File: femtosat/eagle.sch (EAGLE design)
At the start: 21 parts, among them U1 ATMEGA328P_TQFP, U2 915MHz, U3 3.3V/150mA, U4 9DoF IMU, U5 BME280, Y1 16MHz

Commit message: Finished Connecting Sensors
Very unsure if this will work, need to ask lots of questions
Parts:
- added C4, C5: 0.1uF, femtosat:CAPACITOR_0.1UF
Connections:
- removed net N$22: R3.1, TP2.1, U1.PC4(ADC4/SDA)
- removed net N$23: R4.1, TP1.1, U1.PC5(ADC5/SCL)
- removed net N$8: U1.PD2(INT0), U2.DIO0
- new net INT: U1.PD2(INT0), U2.DIO0, U4.INT
- new net N$18: C5.2, U4.REGOUT
- new net SCL: R4.1, TP1.1, U1.PC5(ADC5/SCL), U4.SCL/SCLK, U5.SCK/SCL
- new net SDA: R3.1, TP2.1, U1.PC4(ADC4/SDA), U4.SDA/SDI, U5.SDI/SDA
- net 3.3V: now also C4.2, U4.!CS, U4.VDDIO, U5.!CS, U5.VDDIO
- net GND: now also C4.1, C5.1, U4.AD0/SDO, U4.FSYNC, U5.SDO/ADR
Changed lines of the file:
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@@
 <part name="TP1" library="femtosat" deviceset="TEST-POINT" device="3"/>
 <part name="TP2" library="femtosat" deviceset="TEST-POINT" device="3"/>
+<part name="C4" library="femtosat" deviceset="CAPACITOR_0.1UF" device="" value="0.1uF"/>
+<part name="C5" library="femtosat" deviceset="CAPACITOR_0.1UF" device="" value="0.1uF"/>
 </parts>
 <sheets>
@@
 <attribute name="NAME" x="162.56" y="137.16" size="1.778" layer="95" font="vector" rot="R90"/>
 <attribute name="VALUE" x="167.64" y="137.16" size="1.778" layer="96" font="vector" rot="R90"/>
+</instance>
+<instance part="C4" gate="G$1" x="20.32" y="43.18" smashed="yes" rot="R180">
+<attribute name="NAME" x="18.796" y="40.259" size="1.778" layer="95" font="vector" rot="R180"/>
+<attribute name="VALUE" x="18.796" y="45.339" size="1.778" layer="96" font="vector" rot="R180"/>
+</instance>
+<instance part="C5" gate="G$1" x="25.4" y="30.48" smashed="yes" rot="R180">
+<attribute name="NAME" x="23.876" y="27.559" size="1.778" layer="95" font="vector" rot="R180"/>
+<attribute name="VALUE" x="23.876" y="32.639" size="1.778" layer="96" font="vector" rot="R180"/>
 </instance>
 </instances>
@@
 <pinref part="U4" gate="G$1" pin="GND"/>
 <wire x1="40.64" y1="35.56" x2="30.48" y2="35.56" width="0.1524" layer="91"/>
-<wire x1="30.48" y1="35.56" x2="30.48" y2="20.32" width="0.1524" layer="91"/>
+<wire x1="30.48" y1="35.56" x2="30.48" y2="25.4" width="0.1524" layer="91"/>
 <pinref part="GND9" gate="1" pin="GND"/>
+<pinref part="C4" gate="G$1" pin="1"/>
+<wire x1="30.48" y1="25.4" x2="30.48" y2="20.32" width="0.1524" layer="91"/>
+<wire x1="20.32" y1="38.1" x2="20.32" y2="35.56" width="0.1524" layer="91"/>
+<wire x1="20.32" y1="35.56" x2="30.48" y2="35.56" width="0.1524" layer="91"/>
+<junction x="30.48" y="35.56"/>
+<pinref part="U4" gate="G$1" pin="AD0/SDO"/>
+<wire x1="76.2" y1="35.56" x2="81.28" y2="35.56" width="0.1524" layer="91"/>
+<wire x1="81.28" y1="35.56" x2="81.28" y2="25.4" width="0.1524" layer="91"/>
+<wire x1="81.28" y1="25.4" x2="30.48" y2="25.4" width="0.1524" layer="91"/>
+<junction x="30.48" y="25.4"/>
+<pinref part="C5" gate="G$1" pin="1"/>
+<wire x1="25.4" y1="25.4" x2="30.48" y2="25.4" width="0.1524" layer="91"/>
+<pinref part="U4" gate="G$1" pin="FSYNC"/>
+<wire x1="40.64" y1="40.64" x2="30.48" y2="40.64" width="0.1524" layer="91"/>
+<wire x1="30.48" y1="40.64" x2="30.48" y2="35.56" width="0.1524" layer="91"/>
 </segment>
 <segment>
 <pinref part="U5" gate="U1" pin="GND"/>
 <wire x1="25.4" y1="91.44" x2="20.32" y2="91.44" width="0.1524" layer="91"/>
-<wire x1="20.32" y1="91.44" x2="20.32" y2="81.28" width="0.1524" layer="91"/>
+<wire x1="20.32" y1="91.44" x2="20.32" y2="83.82" width="0.1524" layer="91"/>
 <pinref part="GND10" gate="1" pin="GND"/>
+<pinref part="U5" gate="U1" pin="SDO/ADR"/>
+<wire x1="20.32" y1="83.82" x2="20.32" y2="81.28" width="0.1524" layer="91"/>
+<wire x1="53.34" y1="91.44" x2="58.42" y2="91.44" width="0.1524" layer="91"/>
+<wire x1="58.42" y1="91.44" x2="58.42" y2="83.82" width="0.1524" layer="91"/>
+<wire x1="58.42" y1="83.82" x2="20.32" y2="83.82" width="0.1524" layer="91"/>
+<junction x="20.32" y="83.82"/>
 </segment>
 </net>
@@
 <pinref part="U4" gate="G$1" pin="VDD"/>
 <wire x1="40.64" y1="48.26" x2="30.48" y2="48.26" width="0.1524" layer="91"/>
-<wire x1="30.48" y1="48.26" x2="30.48" y2="58.42" width="0.1524" layer="91"/>
+<wire x1="30.48" y1="48.26" x2="30.48" y2="55.88" width="0.1524" layer="91"/>
 <pinref part="P+4" gate="G$1" pin="3.3V"/>
+<pinref part="U4" gate="G$1" pin="VDDIO"/>
+<wire x1="30.48" y1="55.88" x2="30.48" y2="58.42" width="0.1524" layer="91"/>
+<wire x1="40.64" y1="45.72" x2="30.48" y2="45.72" width="0.1524" layer="91"/>
+<wire x1="30.48" y1="45.72" x2="30.48" y2="48.26" width="0.1524" layer="91"/>
+<junction x="30.48" y="48.26"/>
+<pinref part="C4" gate="G$1" pin="2"/>
+<wire x1="30.48" y1="48.26" x2="20.32" y2="48.26" width="0.1524" layer="91"/>
+<wire x1="20.32" y1="48.26" x2="20.32" y2="45.72" width="0.1524" layer="91"/>
+<pinref part="U4" gate="G$1" pin="!CS"/>
+<wire x1="76.2" y1="43.18" x2="81.28" y2="43.18" width="0.1524" layer="91"/>
+<wire x1="81.28" y1="43.18" x2="81.28" y2="55.88" width="0.1524" layer="91"/>
+<wire x1="81.28" y1="55.88" x2="30.48" y2="55.88" width="0.1524" layer="91"/>
+<junction x="30.48" y="55.88"/>
 </segment>
 <segment>
 <pinref part="U5" gate="U1" pin="VDD"/>
 <wire x1="25.4" y1="104.14" x2="20.32" y2="104.14" width="0.1524" layer="91"/>
-<wire x1="20.32" y1="104.14" x2="20.32" y2="114.3" width="0.1524" layer="91"/>
+<wire x1="20.32" y1="104.14" x2="20.32" y2="109.22" width="0.1524" layer="91"/>
 <pinref part="P+5" gate="G$1" pin="3.3V"/>
+<pinref part="U5" gate="U1" pin="VDDIO"/>
+<wire x1="20.32" y1="109.22" x2="20.32" y2="114.3" width="0.1524" layer="91"/>
+<wire x1="25.4" y1="99.06" x2="20.32" y2="99.06" width="0.1524" layer="91"/>
+<wire x1="20.32" y1="99.06" x2="20.32" y2="104.14" width="0.1524" layer="91"/>
+<junction x="20.32" y="104.14"/>
+<pinref part="U5" gate="U1" pin="!CS"/>
+<wire x1="53.34" y1="104.14" x2="55.88" y2="104.14" width="0.1524" layer="91"/>
+<wire x1="55.88" y1="104.14" x2="55.88" y2="109.22" width="0.1524" layer="91"/>
+<wire x1="55.88" y1="109.22" x2="20.32" y2="109.22" width="0.1524" layer="91"/>
+<junction x="20.32" y="109.22"/>
 </segment>
 <segment>
@@
 </segment>
 </net>
-<net name="N$8" class="0">
+<net name="INT" class="0">
 <segment>
 <pinref part="U1" gate="U$1" pin="PD2(INT0)"/>
@@
 <pinref part="U2" gate="G$1" pin="DIO0"/>
 <wire x1="213.36" y1="96.52" x2="208.28" y2="96.52" width="0.1524" layer="91"/>
+<wire x1="213.36" y1="101.6" x2="220.98" y2="101.6" width="0.1524" layer="91"/>
+<junction x="213.36" y="101.6"/>
+<label x="220.98" y="101.6" size="1.778" layer="95"/>
+</segment>
+<segment>
+<pinref part="U4" gate="G$1" pin="INT"/>
+<wire x1="40.64" y1="43.18" x2="33.02" y2="43.18" width="0.1524" layer="91"/>
+<label x="30.48" y="43.18" size="1.778" layer="95"/>
 </segment>
 </net>
@@
 </segment>
 </net>
-<net name="N$22" class="0">
+<net name="SDA" class="0">
 <segment>
 <pinref part="U1" gate="U$1" pin="PC4(ADC4/SDA)"/>
 <wire x1="154.94" y1="129.54" x2="165.1" y2="129.54" width="0.1524" layer="91"/>
-<wire x1="165.1" y1="129.54" x2="177.8" y2="129.54" width="0.1524" layer="91"/>
+<wire x1="165.1" y1="129.54" x2="172.72" y2="129.54" width="0.1524" layer="91"/>
+<wire x1="172.72" y1="129.54" x2="177.8" y2="129.54" width="0.1524" layer="91"/>
 <wire x1="177.8" y1="129.54" x2="177.8" y2="139.7" width="0.1524" layer="91"/>
 <pinref part="R3" gate="G$1" pin="1"/>
@@
 <wire x1="165.1" y1="139.7" x2="165.1" y2="129.54" width="0.1524" layer="91"/>
 <junction x="165.1" y="129.54"/>
-</segment>
-</net>
-<net name="N$23" class="0">
+<wire x1="172.72" y1="129.54" x2="172.72" y2="134.62" width="0.1524" layer="91"/>
+<junction x="172.72" y="129.54"/>
+<label x="172.72" y="134.62" size="1.778" layer="95" rot="R90"/>
+</segment>
+<segment>
+<pinref part="U4" gate="G$1" pin="SDA/SDI"/>
+<wire x1="76.2" y1="38.1" x2="86.36" y2="38.1" width="0.1524" layer="91"/>
+<label x="86.36" y="38.1" size="1.778" layer="95"/>
+</segment>
+<segment>
+<pinref part="U5" gate="U1" pin="SDI/SDA"/>
+<wire x1="53.34" y1="99.06" x2="58.42" y2="99.06" width="0.1524" layer="91"/>
+<label x="58.42" y="99.06" size="1.778" layer="95"/>
+</segment>
+</net>
+<net name="SCL" class="0">
 <segment>
 <pinref part="U1" gate="U$1" pin="PC5(ADC5/SCL)"/>
@@
 <wire x1="187.96" y1="134.62" x2="187.96" y2="127" width="0.1524" layer="91"/>
 <junction x="187.96" y="127"/>
-</segment>
-</net>
+<wire x1="195.58" y1="127" x2="203.2" y2="127" width="0.1524" layer="91"/>
+<junction x="195.58" y="127"/>
+<label x="203.2" y="127" size="1.778" layer="95"/>
+</segment>
+<segment>
+<pinref part="U4" gate="G$1" pin="SCL/SCLK"/>
+<wire x1="76.2" y1="40.64" x2="86.36" y2="40.64" width="0.1524" layer="91"/>
+<label x="86.36" y="40.64" size="1.778" layer="95"/>
+</segment>
+<segment>
+<pinref part="U5" gate="U1" pin="SCK/SCL"/>
+<wire x1="53.34" y1="96.52" x2="58.42" y2="96.52" width="0.1524" layer="91"/>
+<label x="58.42" y="96.52" size="1.778" layer="95"/>
+</segment>
+</net>
+<net name="N$18" class="0">
+<segment>
+<pinref part="U4" gate="G$1" pin="REGOUT"/>
+<wire x1="40.64" y1="38.1" x2="25.4" y2="38.1" width="0.1524" layer="91"/>
+<pinref part="C5" gate="G$1" pin="2"/>
+<wire x1="25.4" y1="38.1" x2="25.4" y2="33.02" width="0.1524" layer="91"/>
+</segment>
+</net>

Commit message: Corrected Capacitors and Resistors
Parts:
- added C6, C7: 0.1uF, femtosat:CAPACITOR_0.1UF
- added R10, R8, R9: 10K, femtosat:RESISTOR_10KOHM0603
- added R11, R6, R7: 4.7k, femtosat:RESISTOR_4.7KOHM-0603-1/10W-1%
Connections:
- new net N$16: R11.2, U5.!CS
- new net N$8: R8.1, U4.!CS
- net 3.3V: now also C6.1, C7.1, R10.2, R11.1, R6.2, R7.2, R8.2, R9.2; no longer U4.!CS, U5.!CS
- net GND: now also C6.2, C7.2, U4.INT
- net INT: no longer U4.INT
- net SCL: now also R6.1, R9.1
- net SDA: now also R10.1, R7.1

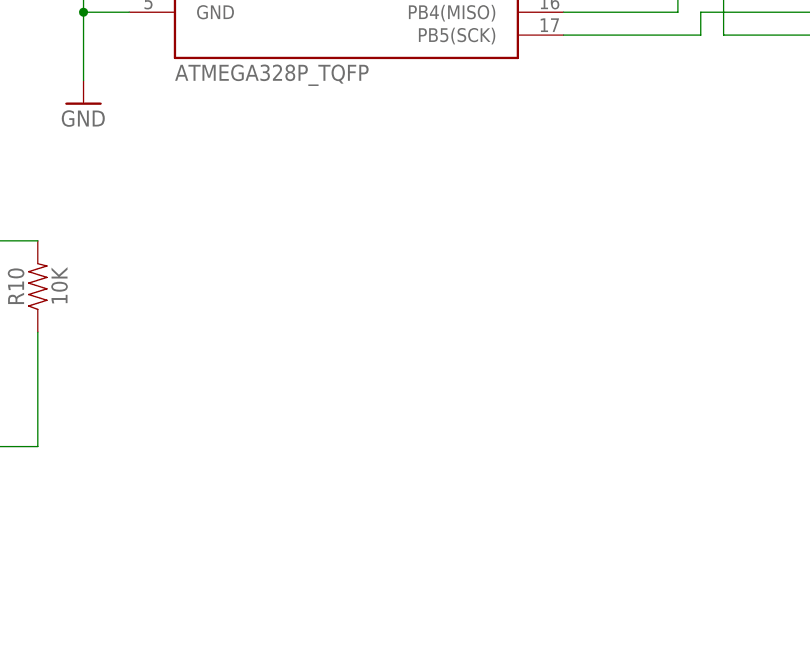
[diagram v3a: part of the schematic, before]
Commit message: Added Memory Module
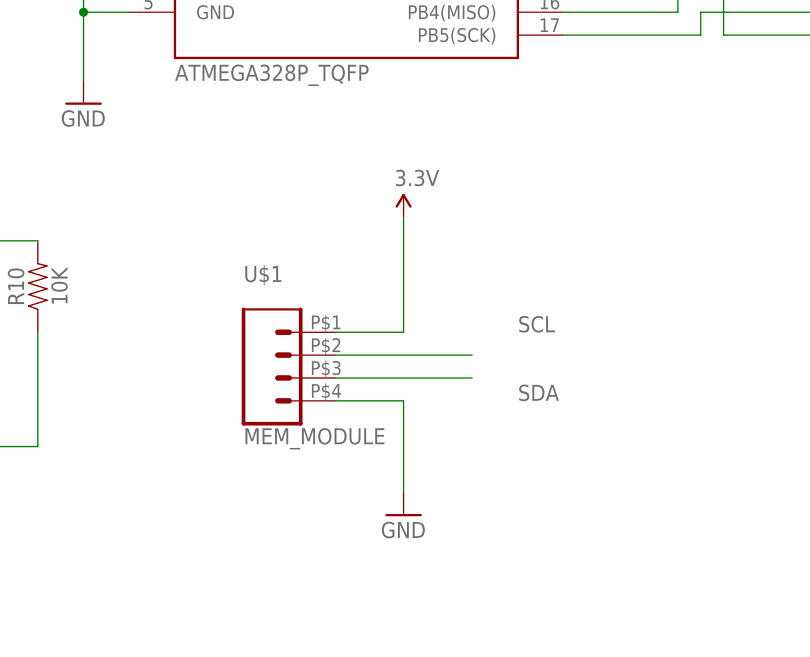
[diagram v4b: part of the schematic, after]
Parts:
- added U$1: MEM_MODULE, femtosat:MEM_MODULE
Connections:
- net 3.3V: now also U$1.4
- net GND: now also U$1.1
- net SCL: now also U$1.3
- net SDA: now also U$1.2
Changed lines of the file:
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@@
 <part name="R10" library="femtosat" deviceset="RESISTOR_10KOHM" device="0603" value="10K"/>
 <part name="R11" library="femtosat" deviceset="RESISTOR_4.7KOHM" device="-0603-1/10W-1%" value="4.7k"/>
+<part name="U$1" library="femtosat" deviceset="MEM_MODULE" device=""/>
+<part name="P+7" library="femtosat" deviceset="3.3V" device=""/>
+<part name="GND11" library="femtosat" deviceset="GND" device=""/>
 </parts>
 <sheets>
@@
 <attribute name="NAME" x="50.8" y="110.744" size="1.778" layer="95" font="vector" align="bottom-center"/>
 <attribute name="VALUE" x="50.8" y="107.696" size="1.778" layer="96" font="vector" align="top-center"/>
+</instance>
+<instance part="U$1" gate="G$1" x="121.92" y="45.72" smashed="yes">
+<attribute name="VALUE" x="119.38" y="35.814" size="1.778" layer="96" font="vector"/>
+<attribute name="NAME" x="119.38" y="53.848" size="1.778" layer="95" font="vector"/>
+</instance>
+<instance part="P+7" gate="G$1" x="137.16" y="60.96" smashed="yes">
+<attribute name="VALUE" x="136.144" y="64.516" size="1.778" layer="96"/>
+</instance>
+<instance part="GND11" gate="1" x="137.16" y="27.94" smashed="yes">
+<attribute name="VALUE" x="134.62" y="25.4" size="1.778" layer="96"/>
 </instance>
 </instances>
@@
 <wire x1="17.78" y1="88.9" x2="20.32" y2="88.9" width="0.1524" layer="91"/>
 <junction x="20.32" y="88.9"/>
+</segment>
+<segment>
+<pinref part="U$1" gate="G$1" pin="1"/>
+<wire x1="129.54" y1="40.64" x2="137.16" y2="40.64" width="0.1524" layer="91"/>
+<wire x1="137.16" y1="40.64" x2="137.16" y2="30.48" width="0.1524" layer="91"/>
+<pinref part="GND11" gate="1" pin="GND"/>
 </segment>
 </net>
@@
 <pinref part="P+6" gate="G$1" pin="3.3V"/>
 </segment>
+<segment>
+<pinref part="U$1" gate="G$1" pin="4"/>
+<wire x1="129.54" y1="48.26" x2="137.16" y2="48.26" width="0.1524" layer="91"/>
+<wire x1="137.16" y1="48.26" x2="137.16" y2="60.96" width="0.1524" layer="91"/>
+<pinref part="P+7" gate="G$1" pin="3.3V"/>
+</segment>
 </net>
 <net name="INT" class="0">
@@
 <junction x="55.88" y="99.06"/>
 </segment>
+<segment>
+<pinref part="U$1" gate="G$1" pin="2"/>
+<wire x1="129.54" y1="43.18" x2="144.78" y2="43.18" width="0.1524" layer="91"/>
+<label x="149.86" y="40.64" size="1.778" layer="95"/>
+</segment>
 </net>
 <net name="SCL" class="0">
@@
 <junction x="55.88" y="96.52"/>
 </segment>
-</net>
+<segment>
+<pinref part="U$1" gate="G$1" pin="3"/>
+<wire x1="129.54" y1="45.72" x2="144.78" y2="45.72" width="0.1524" layer="91"/>
+<label x="149.86" y="48.26" size="1.778" layer="95"/>
+</segment>
+</net>

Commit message: Passoff Fixes
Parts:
- removed C4, C6, C7: 0.1uF, femtosat:CAPACITOR_0.1UF
- removed R10, R8, R9: 10K, femtosat:RESISTOR_10KOHM0603
- removed R11, R6, R7: 4.7k, femtosat:RESISTOR_4.7KOHM-0603-1/10W-1%
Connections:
- removed net N$16: R11.2, U5.!CS
- removed net N$8: R8.1, U4.!CS
- net 3.3V: no longer C4.2, C6.1, C7.1, R10.2, R11.1, R6.2, R7.2, R8.2, R9.2
- net GND: no longer C4.1, C6.2, C7.2, U4.INT
- net SCL: no longer R6.1, R9.1
- net SDA: no longer R10.1, R7.1
